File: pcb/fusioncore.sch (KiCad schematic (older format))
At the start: 125 parts, among them J1 40HAT, J10 Pump_Misc_1, J11 Pump_Misc_2, J12 I2C_DBG, J13 Conn_02x03_Top_Bottom, J14 LED, J15 Trigger, J16 WEIGHT, J17 Valve_M1, J18 Valve_M2, J19 Valve_M3, J2 Conn_02x12_Top_Bottom, J20 Valve_M4, J21 Valve_Air_Lime, J22 Valve_Air_Rum, J23 Valve_Air_Out, J24 Cooling_Copressor, J3 Flow_Warm, J4 Temperature, J5 Flow_Cold, J6 WEIGHT_B, J7 Pump_Cold, J8 Pump_Warm, J9 Pump_Air, K1 G5Q-1A, Q1 DMG2305UX, Q10 AO3400A, Q11 AO3400A, Q12 2N3904, Q2 DMMT5401, Q3 AO3400A, Q4 AO3400A, Q5 AO3400A, Q6 AO3400A, Q7 AO3400A, Q8 MMBT4403, Q9 AO3400A, SW1 POWER_ON, U1 CAT24C32, U2 INA226, U3 INA226, U4 INA226, U5 TXB0108DQSR, U6 HX711, U7 P82B96

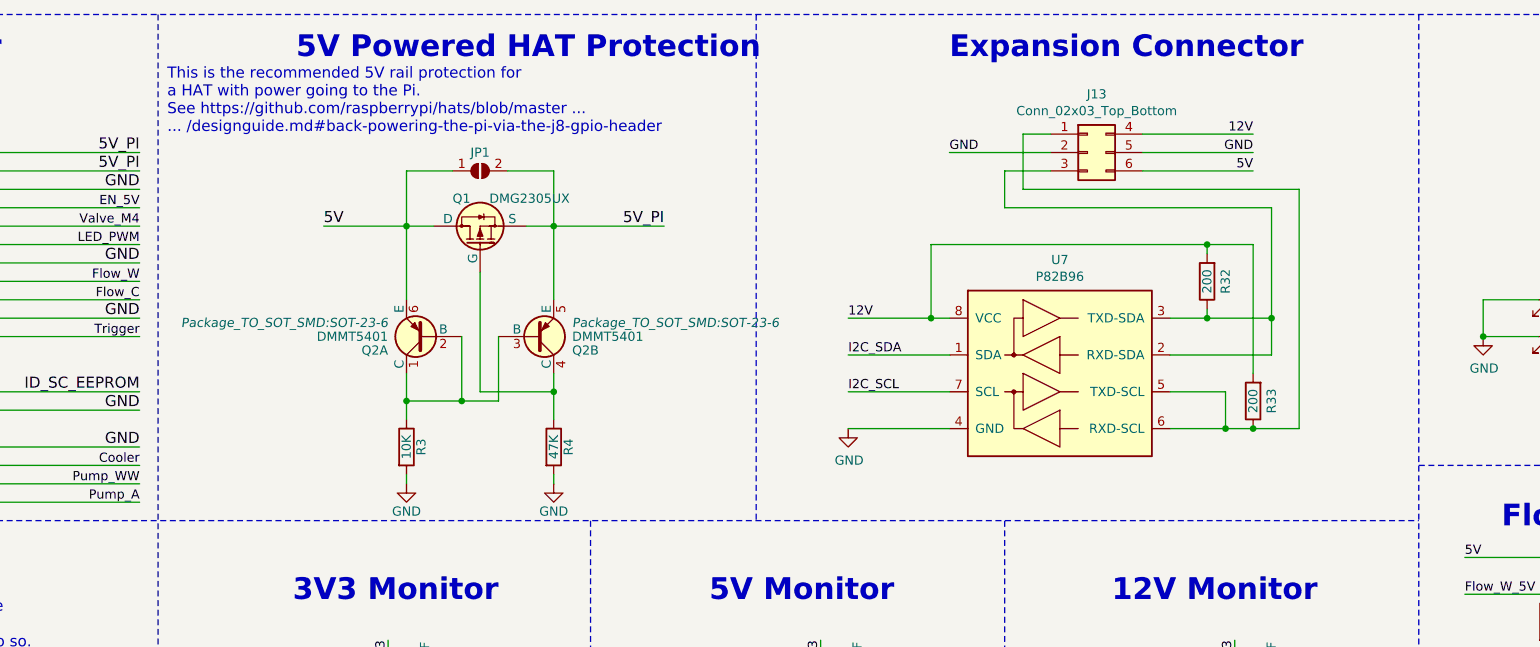
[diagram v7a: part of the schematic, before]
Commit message: Added jumper to allow switching I2C voltage on expansion connector.
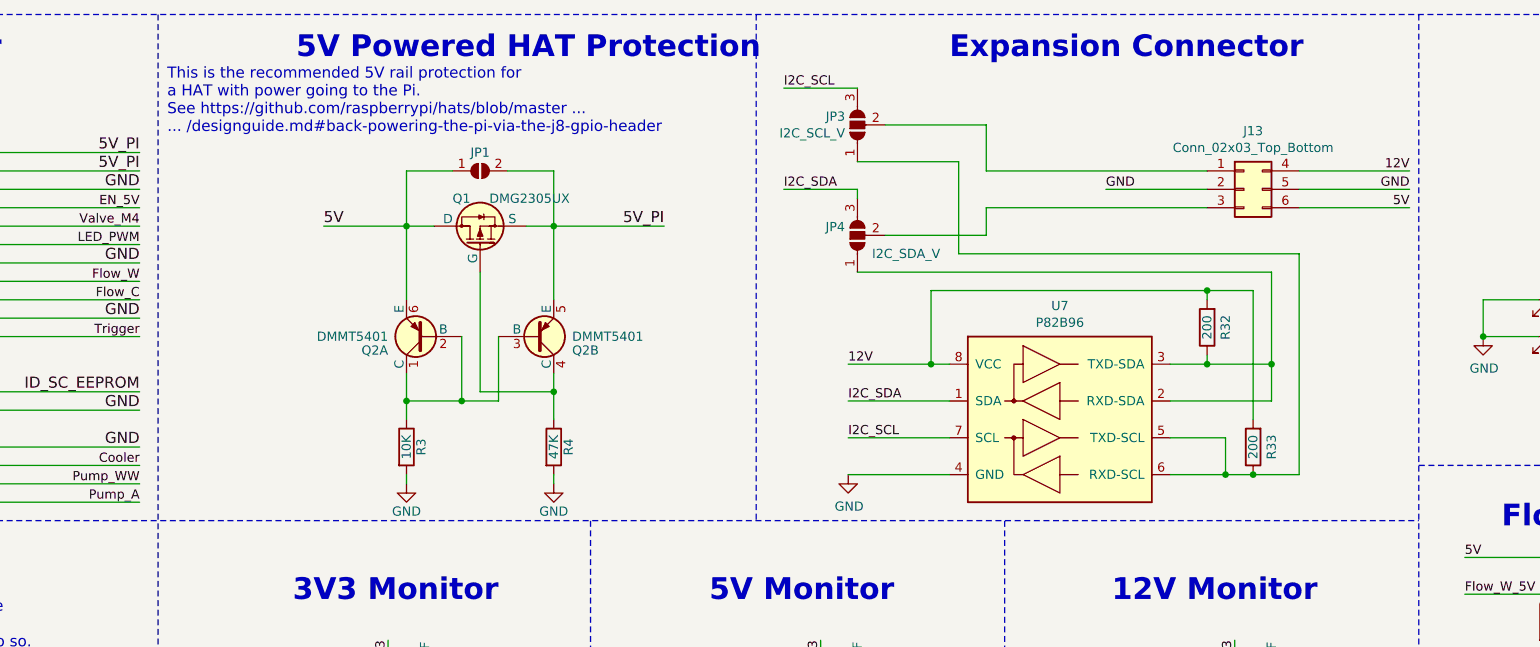
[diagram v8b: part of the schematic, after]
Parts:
- added JP3: I2C_SCL_V, Jumper:SolderJumper-3_P1.3mm_Open_Pad1.0x1.5mm, symbol Jumper:SolderJumper_3_Open
- added JP4: I2C_SDA_V, Jumper:SolderJumper-3_P1.3mm_Open_Pad1.0x1.5mm, symbol Jumper:SolderJumper_3_Open
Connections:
- net I2C_SCL: now also JP3.3 (B)
- net I2C_SDA: now also JP4.3 (B)
- net at R32.1, U7.2 (RXD-SDA), U7.3 (TXD-SDA): now also JP4.1 (A); no longer J13.3 (Pin_3)
- net at R33.1, U7.5 (TXD-SCL), U7.6 (RXD-SCL): now also JP3.1 (A); no longer J13.1 (Pin_1)
- new net: J13.1 (Pin_1), JP3.2 (C)
- new net: J13.3 (Pin_3), JP4.2 (C)
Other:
- moved on the sheet: J13, R32, R33, U7
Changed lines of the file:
@@
 F 0 "Q2" H 6050 2325 50  0000 L CNN
 F 1 "DMMT5401" H 6050 2250 50  0000 L CNN
-F 2 "Package_TO_SOT_SMD:SOT-23-6" H 6050 2175 50  0000 L CIN
+F 2 "Package_TO_SOT_SMD:SOT-23-6" H 6050 2175 50  0001 L CIN
 F 3 "" H 5850 2250 50  0000 L CNN
 F 4 "C154733" H 5850 2250 50  0001 C CNN "LCSC"
@@
 F 0 "Q2" H 6650 2325 50  0000 L CNN
 F 1 "DMMT5401" H 6650 2250 50  0000 L CNN
-F 2 "Package_TO_SOT_SMD:SOT-23-6" H 6650 2175 50  0000 L CIN
+F 2 "Package_TO_SOT_SMD:SOT-23-6" H 6650 2175 50  0001 L CIN
 F 3 "" H 6450 2250 50  0000 L CNN
 F 4 "C154733" H 6450 2250 50  0001 C CNN "LCSC"
@@
 Expansion Connector
 Wire Wire Line
-	8700 2550 8150 2550
+	8700 2800 8150 2800
 Wire Wire Line
-	9250 1250 8700 1250
+	10100 1450 9550 1450
 Wire Wire Line
-	8700 2350 8150 2350
+	8700 2600 8150 2600
 Wire Wire Line
-	9750 1350 10350 1350
+	10600 1550 11200 1550
 Wire Wire Line
-	9750 1250 10350 1250
-Text Label 8150 2550 0    50   ~ 0
+	10600 1450 11200 1450
+Text Label 8150 2800 0    50   ~ 0
 I2C_SCL
-Text Label 8150 2350 0    50   ~ 0
+Text Label 8150 2600 0    50   ~ 0
 I2C_SDA
-Text Label 10350 1350 2    50   ~ 0
+Text Label 11200 1550 2    50   ~ 0
 5V
-Text Label 10350 1150 2    50   ~ 0
+Text Label 11200 1350 2    50   ~ 0
 12V
-Text Label 10350 1250 2    50   ~ 0
+Text Label 11200 1450 2    50   ~ 0
 GND
-Text Label 8700 1250 0    50   ~ 0
+Text Label 9550 1450 0    50   ~ 0
 GND
 Wire Wire Line
-	9750 1150 10350 1150
+	10600 1350 11200 1350
 $Comp
 L Connector_Generic:Conn_01x04 J12
@@
 L Interface_Expansion:P82B96 U7
 U 1 1 5E3F0F69
-P 9300 2450
-F 0 "U7" H 9300 3067 50  0000 C CNN
-F 1 "P82B96" H 9300 2976 50  0000 C CNN
-F 2 "Package_SO:SOIC-8_3.9x4.9mm_P1.27mm" H 9300 2450 50  0001 C CNN
-F 3 "http://www.nxp.com/documents/data_sheet/P82B96.pdf" H 9300 2450 50  0001 C CNN
-F 4 "C32103" H 9300 2450 50  0001 C CNN "LCSC"
-	1    9300 2450
+P 9300 2700
+F 0 "U7" H 9300 3317 50  0000 C CNN
+F 1 "P82B96" H 9300 3226 50  0000 C CNN
+F 2 "Package_SO:SOIC-8_3.9x4.9mm_P1.27mm" H 9300 2700 50  0001 C CNN
+F 3 "http://www.nxp.com/documents/data_sheet/P82B96.pdf" H 9300 2700 50  0001 C CNN
+F 4 "C32103" H 9300 2700 50  0001 C CNN "LCSC"
+	1    9300 2700
 	1    0    0    -1
 $EndComp
 Wire Wire Line
-	8700 2150 8600 2150
+	8700 2400 8600 2400
 Wire Wire Line
-	8700 2750 8150 2750
+	8700 3000 8150 3000
 $Comp
 L power:GND #PWR0102
 U 1 1 5E56E556
-P 8150 2750
-F 0 "#PWR0102" H 8150 2500 50  0001 C CNN
-F 1 "GND" H 8155 2577 50  0000 C CNN
-F 2 "" H 8150 2750 50  0001 C CNN
-F 3 "" H 8150 2750 50  0001 C CNN
-	1    8150 2750
+P 8150 3000
+F 0 "#PWR0102" H 8150 2750 50  0001 C CNN
+F 1 "GND" H 8155 2827 50  0000 C CNN
+F 2 "" H 8150 3000 50  0001 C CNN
+F 3 "" H 8150 3000 50  0001 C CNN
+	1    8150 3000
 	1    0    0    -1
 $EndComp
-Text Label 8150 2150 0    50   ~ 0
+Text Label 8150 2400 0    50   ~ 0
 12V
 Wire Wire Line
-	8600 2150 8600 1750
+	8600 2400 8600 2000
 Wire Wire Line
-	8600 1750 10100 1750
-Connection ~ 8600 2150
+	8600 2000 10100 2000
+Connection ~ 8600 2400
 Wire Wire Line
-	8600 2150 8150 2150
+	8600 2400 8150 2400
 $Comp
 L Device:R R32
 U 1 1 5E5F342B
-P 10100 1950
-F 0 "R32" V 10000 1950 50  0000 C CNN
-F 1 "200" V 10100 1950 50  0000 C CNN
-F 2 "Resistor_SMD:R_0805_2012Metric_Pad1.15x1.40mm_HandSolder" V 10030 1950 50  0001 C CNN
-F 3 "~" H 10100 1950 50  0001 C CNN
-F 4 "C17540" V 10100 1950 50  0001 C CNN "LCSC"
-	1    10100 1950
+P 10100 2200
+F 0 "R32" V 10000 2200 50  0000 C CNN
+F 1 "200" V 10100 2200 50  0000 C CNN
+F 2 "Resistor_SMD:R_0805_2012Metric_Pad1.15x1.40mm_HandSolder" V 10030 2200 50  0001 C CNN
+F 3 "~" H 10100 2200 50  0001 C CNN
+F 4 "C17540" V 10100 2200 50  0001 C CNN "LCSC"
+	1    10100 2200
 	-1   0    0    1
 $EndComp
 Wire Wire Line
-	10100 1750 10100 1800
+	10100 2000 10100 2050
 Wire Wire Line
-	10100 2100 10100 2150
-Connection ~ 10100 2150
+	10100 2350 10100 2400
+Connection ~ 10100 2400
 Wire Wire Line
-	10100 2150 9900 2150
+	10100 2400 9900 2400
 $Comp
 L Device:R R33
 U 1 1 5E7C51B3
-P 10350 2600
-F 0 "R33" V 10250 2600 50  0000 C CNN
-F 1 "200" V 10350 2600 50  0000 C CNN
-F 2 "Resistor_SMD:R_0805_2012Metric_Pad1.15x1.40mm_HandSolder" V 10280 2600 50  0001 C CNN
-F 3 "~" H 10350 2600 50  0001 C CNN
-F 4 "C17540" V 10350 2600 50  0001 C CNN "LCSC"
-	1    10350 2600
+P 10350 2850
+F 0 "R33" V 10250 2850 50  0000 C CNN
+F 1 "200" V 10350 2850 50  0000 C CNN
+F 2 "Resistor_SMD:R_0805_2012Metric_Pad1.15x1.40mm_HandSolder" V 10280 2850 50  0001 C CNN
+F 3 "~" H 10350 2850 50  0001 C CNN
+F 4 "C17540" V 10350 2850 50  0001 C CNN "LCSC"
+	1    10350 2850
 	-1   0    0    1
 $EndComp
-Connection ~ 10350 2750
+Connection ~ 10350 3000
 Wire Wire Line
-	10100 2150 10450 2150
+	10100 2400 10450 2400
 Wire Wire Line
-	9900 2750 10200 2750
+	9900 3000 10200 3000
 Wire Wire Line
-	9900 2350 10450 2350
+	9900 2600 10450 2600
 Wire Wire Line
-	10100 1750 10350 1750
+	10100 2000 10350 2000
 Wire Wire Line
-	10350 1750 10350 2450
-Connection ~ 10100 1750
+	10350 2000 10350 2700
+Connection ~ 10100 2000
 Wire Wire Line
-	10450 2350 10450 2150
+	10450 2600 10450 2400
 Wire Wire Line
-	10450 1550 10450 2150
-Connection ~ 10450 2150
-Wire Wire Line
-	10600 2750 10600 1450
-Wire Wire Line
-	10350 2750 10600 2750
+	10350 3000 10600 3000
 $Comp
 L Connector_Generic:Conn_02x03_Top_Bottom J13
 U 1 1 5E55E4B6
-P 9450 1250
-F 0 "J13" H 9500 1567 50  0000 C CNN
-F 1 "Conn_02x03_Top_Bottom" H 9500 1476 50  0000 C CNN
-F 2 "Connector_Molex:Molex_Micro-Fit_3.0_43045-0612_2x03_P3.00mm_Vertical" H 9450 1250 50  0001 C CNN
-F 3 "https://www.molex.com/pdm_docs/sd/430450612_sd.pdf" H 9450 1250 50  0001 C CNN
-F 4 "WM1791-ND " H 9450 1250 50  0001 C CNN "Digikey"
-	1    9450 1250
+P 10300 1450
+F 0 "J13" H 10350 1767 50  0000 C CNN
+F 1 "Conn_02x03_Top_Bottom" H 10350 1676 50  0000 C CNN
+F 2 "Connector_Molex:Molex_Micro-Fit_3.0_43045-0612_2x03_P3.00mm_Vertical" H 10300 1450 50  0001 C CNN
+F 3 "https://www.molex.com/pdm_docs/sd/430450612_sd.pdf" H 10300 1450 50  0001 C CNN
+F 4 "WM1791-ND " H 10300 1450 50  0001 C CNN "Digikey"
+	1    10300 1450
 	1    0    0    -1
 $EndComp
 Wire Wire Line
-	9100 1450 9100 1150
-Wire Wire Line
-	9100 1150 9250 1150
-Wire Wire Line
-	9100 1450 10600 1450
-Wire Wire Line
-	9000 1550 9000 1350
-Wire Wire Line
-	9000 1350 9250 1350
-Wire Wire Line
-	9000 1550 10450 1550
-Wire Wire Line
-	9900 2550 10200 2550
+	9900 2800 10200 2800
 Wire Wire Line
-	10200 2550 10200 2750
-Connection ~ 10200 2750
+	10200 2800 10200 3000
+Connection ~ 10200 3000
 Wire Wire Line
-	10200 2750 10350 2750
+	10200 3000 10350 3000
 NoConn ~ 15450 1550
 Wire Wire Line
@@
 Wire Wire Line
 	6500 8700 6400 8700
+$Comp
+L Jumper:SolderJumper_3_Open JP3
+U 1 1 5E7A9CBF
+P 8200 1100
+F 0 "JP3" V 8246 1167 50  0000 L CNN
+F 1 "I2C_SCL_V" V 8155 1167 50  0000 L CNN
+F 2 "Jumper:SolderJumper-3_P1.3mm_Open_Pad1.0x1.5mm" H 8200 1100 50  0001 C CNN
+F 3 "~" H 8200 1100 50  0001 C CNN
+	1    8200 1100
+	0    -1   -1   0
+$EndComp
+$Comp
+L Jumper:SolderJumper_3_Open JP4
+U 1 1 5EB2D88F
+P 8200 1700
+F 0 "JP4" V 8246 1768 50  0000 L CNN
+F 1 "I2C_SDA_V" V 8100 1250 50  0000 L CNN
+F 2 "Jumper:SolderJumper-3_P1.3mm_Open_Pad1.0x1.5mm" H 8200 1700 50  0001 C CNN
+F 3 "~" H 8200 1700 50  0001 C CNN
+	1    8200 1700
+	0    -1   -1   0
+$EndComp
+Wire Wire Line
+	10100 1350 8900 1350
+Wire Wire Line
+	8900 1350 8900 1100
+Wire Wire Line
+	8900 1100 8350 1100
+Wire Wire Line
+	10100 1550 8900 1550
+Wire Wire Line
+	8900 1550 8900 1700
+Wire Wire Line
+	8350 1700 8900 1700
+Wire Wire Line
+	10450 2400 10450 1900
+Wire Wire Line
+	10450 1900 8200 1900
+Connection ~ 10450 2400
+Wire Wire Line
+	8200 1300 8750 1300
+Wire Wire Line
+	8750 1300 8750 1800
+Wire Wire Line
+	8750 1800 10600 1800
+Wire Wire Line
+	10600 1800 10600 3000
+Wire Wire Line
+	8200 1500 8200 1450
+Wire Wire Line
+	8200 1450 7800 1450
+Text Label 7800 1450 0    50   ~ 0
+I2C_SDA
+Wire Wire Line
+	8200 900  7800 900
+Text Label 7800 900  0    50   ~ 0
+I2C_SCL
 $EndSCHEMATC
